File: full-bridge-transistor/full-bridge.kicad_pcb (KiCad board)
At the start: 2 copper layers, 97.8 x 98 mm, 42 parts, among them J1 Screw_Terminal_01x02, J10 Conn_01x01, J11 Conn_01x01, J12 Conn_01x01, J2 Screw_Terminal_01x02, J3 Bridge1, J4 Screw_Terminal_01x02, J5 Screw_Terminal_01x02, J6 Bridge2, J7 NegBus, J8 PosBus, J9 Conn_01x01, Q1 Q_NIGBT_GCE, Q2 Q_NIGBT_GCE, Q3 Q_NIGBT_GCE, Q4 Q_NIGBT_GCE

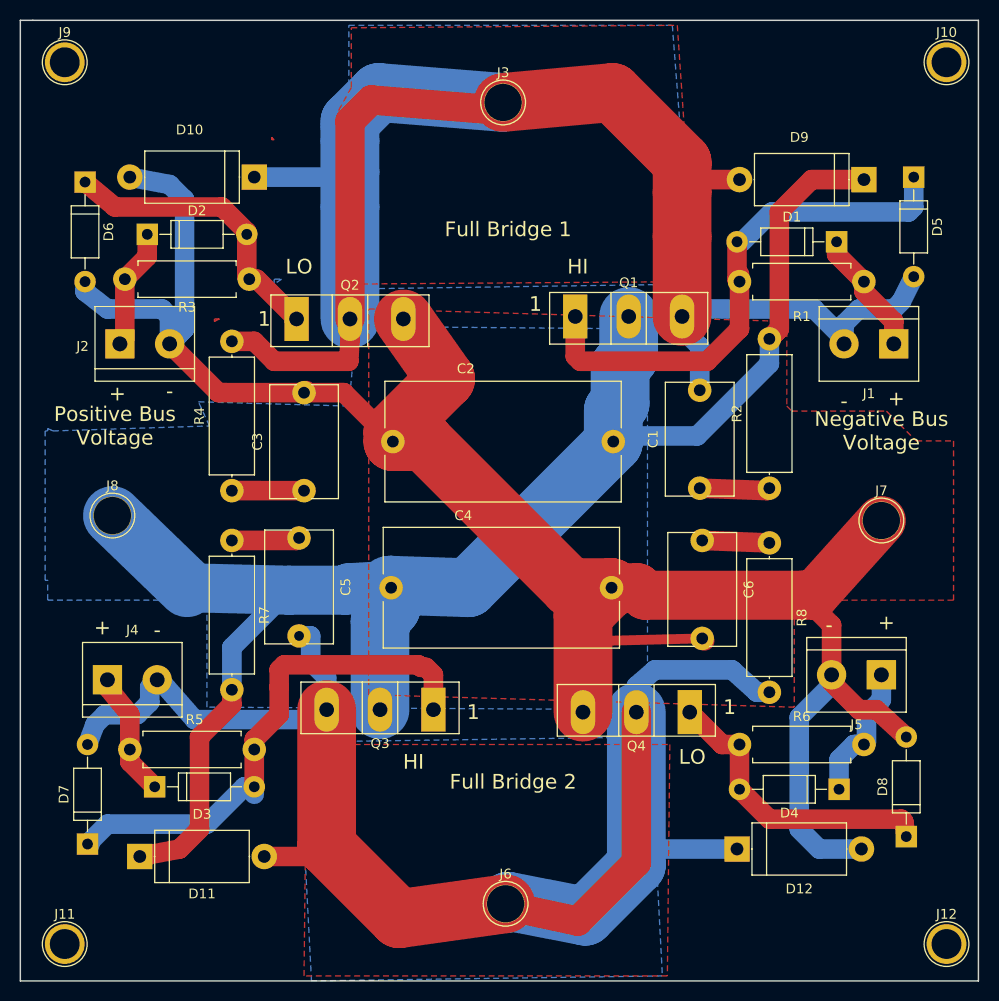
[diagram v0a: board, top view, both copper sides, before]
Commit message: Cleaned up labels and pads on half/full bridge boards
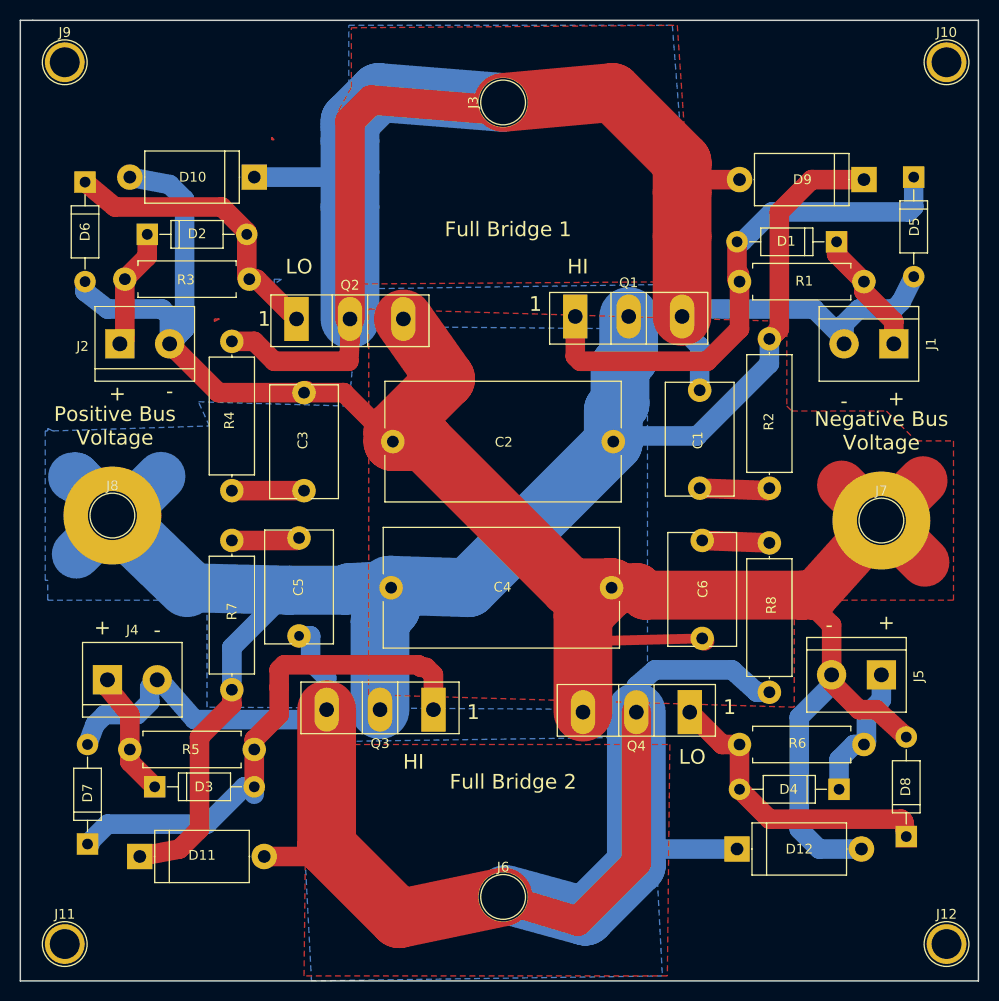
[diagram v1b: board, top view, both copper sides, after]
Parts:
- moved J6 0.74 mm to (94.7, 135.2)
- turned J3 to 90 degrees
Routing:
- net VDD: track 169.7 -> 187.6 mm
- net GND: track 221.5 -> 239.0 mm
- net Net-(C5-Pad2): track 209.2 -> 209.8 mm

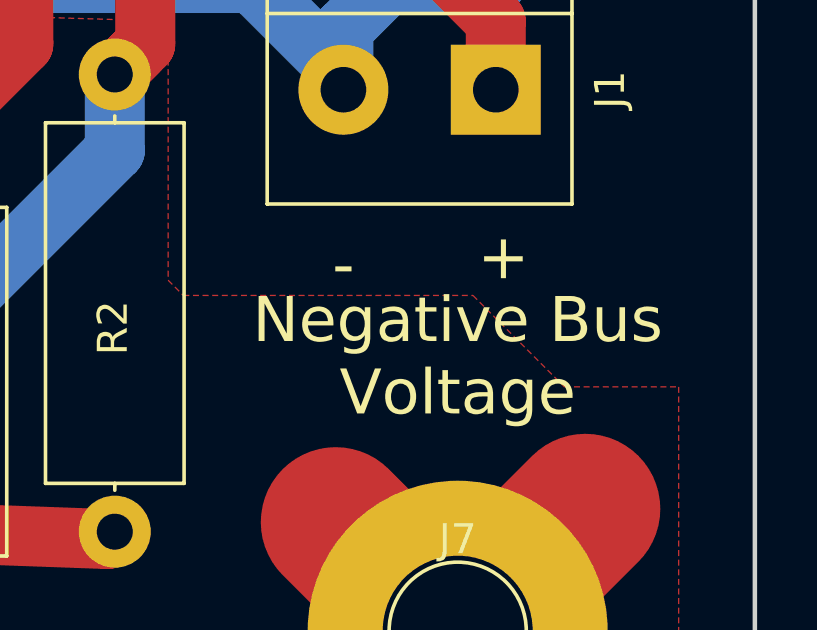
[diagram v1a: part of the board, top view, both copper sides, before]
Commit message: Added optional frequency halving to ensure 50% duty cycle
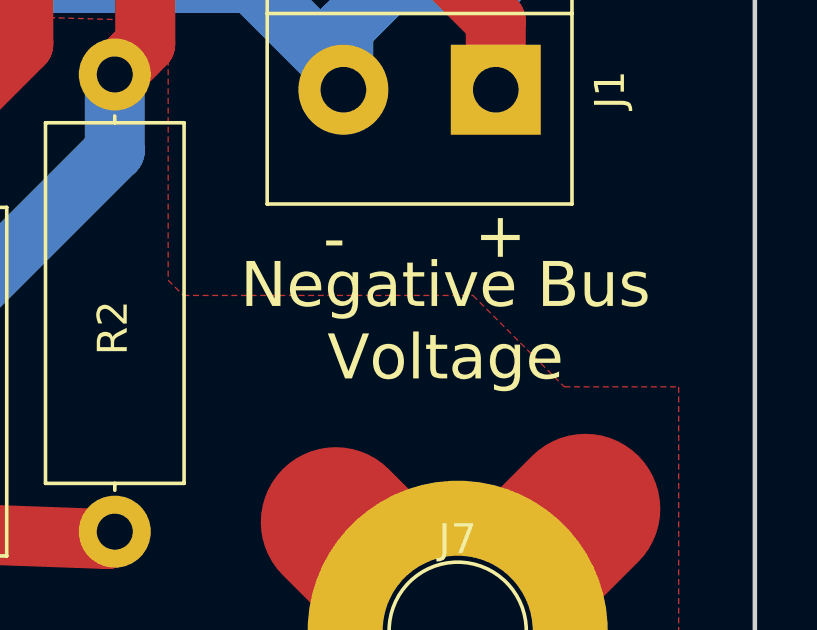
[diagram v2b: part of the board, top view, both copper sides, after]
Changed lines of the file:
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@@
     (links 60)
     (no_connects 0)
-    (area 45.252381 45.644999 144.74762 144.075)
+    (area 45.390999 45.644999 143.331001 143.839001)
     (thickness 1.6)
     (drawings 25)
@@
   )
   (setup
-    (last_trace_width 5)
+    (last_trace_width 0.25)
     (user_trace_width 1)
     (user_trace_width 2)
@@
   (gr_line (start 143.256 45.72) (end 143.256 143.764) (angle 90) (layer Edge.Cuts) (width 0.15))
   (gr_line (start 46.736 45.72) (end 143.256 45.72) (angle 90) (layer Edge.Cuts) (width 0.15))
-  (gr_text - (at 129.54 84.582) (layer F.SilkS)
+  (gr_text - (at 129.2352 83.7184) (layer F.SilkS)
     (effects (font (size 1.5 1.5) (thickness 0.3)))
   )
@@
     (effects (font (size 1.5 1.5) (thickness 0.3)))
   )
-  (gr_text + (at 134.874 84.328) (layer F.SilkS)
+  (gr_text + (at 134.7724 83.6168) (layer F.SilkS)
     (effects (font (size 1.5 1.5) (thickness 0.3)))
   )
@@
     (effects (font (size 1.5 1.5) (thickness 0.3)))
   )
-  (gr_text "Negative Bus\nVoltage" (at 133.35 87.63) (layer F.SilkS)
-    (effects (font (size 1.5 1.5) (thickness 0.3)))
-  )
+  (gr_text "Negative Bus\nVoltage" (at 132.9436 86.4616) (layer F.SilkS)
+    (effects (font (size 1.5 1.5) (thickness 0.3)))
+  )
